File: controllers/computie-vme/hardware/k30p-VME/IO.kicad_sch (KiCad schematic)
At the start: 44 parts, among them J4 Serial1, J5 Serial2, P1 USB_C_Plug_USB2.0, P2 USB_C_Plug_USB2.0, SW3 E-Switch TL2243, U10 FT231XS, U3 74HC05, U8 MC68681, U9 FT231XS, Y2 Crystal

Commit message: Updating with more work in progress
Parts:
- removed JP2: IRQ, Connector_PinHeader_2.54mm:PinHeader_1x02_P2.54mm_Vertical, symbol Jumper:Jumper_2_Open
- removed JP3: ~{IACK}, Connector_PinHeader_2.54mm:PinHeader_1x02_P2.54mm_Vertical, symbol Jumper:Jumper_2_Open
- removed U3: 74HC05, Package_SO:TSSOP-14_4.4x5mm_P0.65mm, symbol 74xx:74LS05
- L1: value 600Ω @ 100MHz (MI0805K601R-10) -> MI0805K601R-10
- renumbered D5 to D2, D6 to D3, D3 to D4, D4 to D5, D7 to D6, D8 to D7, R16 to R12, R17 to R13, R18 to R14, R19 to R15, R12 to R16, R13 to R17, R14 to R18, R15 to R19, SW3 to SW2, P1 to USB1, P2 to USB2
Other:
- note added: "600Ω @ 100MHz"
- note added: "MC68681 DUAL SERIAL PORT CONTROLLER"
- note added: "SERIAL #1 FTDI SERIAL-TO-USB ADAPTER"
- note added: "SERIAL #2 FTDI SERIAL-TO-USB ADAPTER"
- note added: "TTL-LEVEL SERIAL DEBUG HEADERS"
- note removed: "TODO: remove these jumpers, rename the wires and use the priority encoder from the VME bus to generate the interrupts?"
- title: k30-VME32 -> k30p-VME
- moved on the sheet: C10, C11, C4, C5, C6, C7, C8, C9, D2, D3, D4, D5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

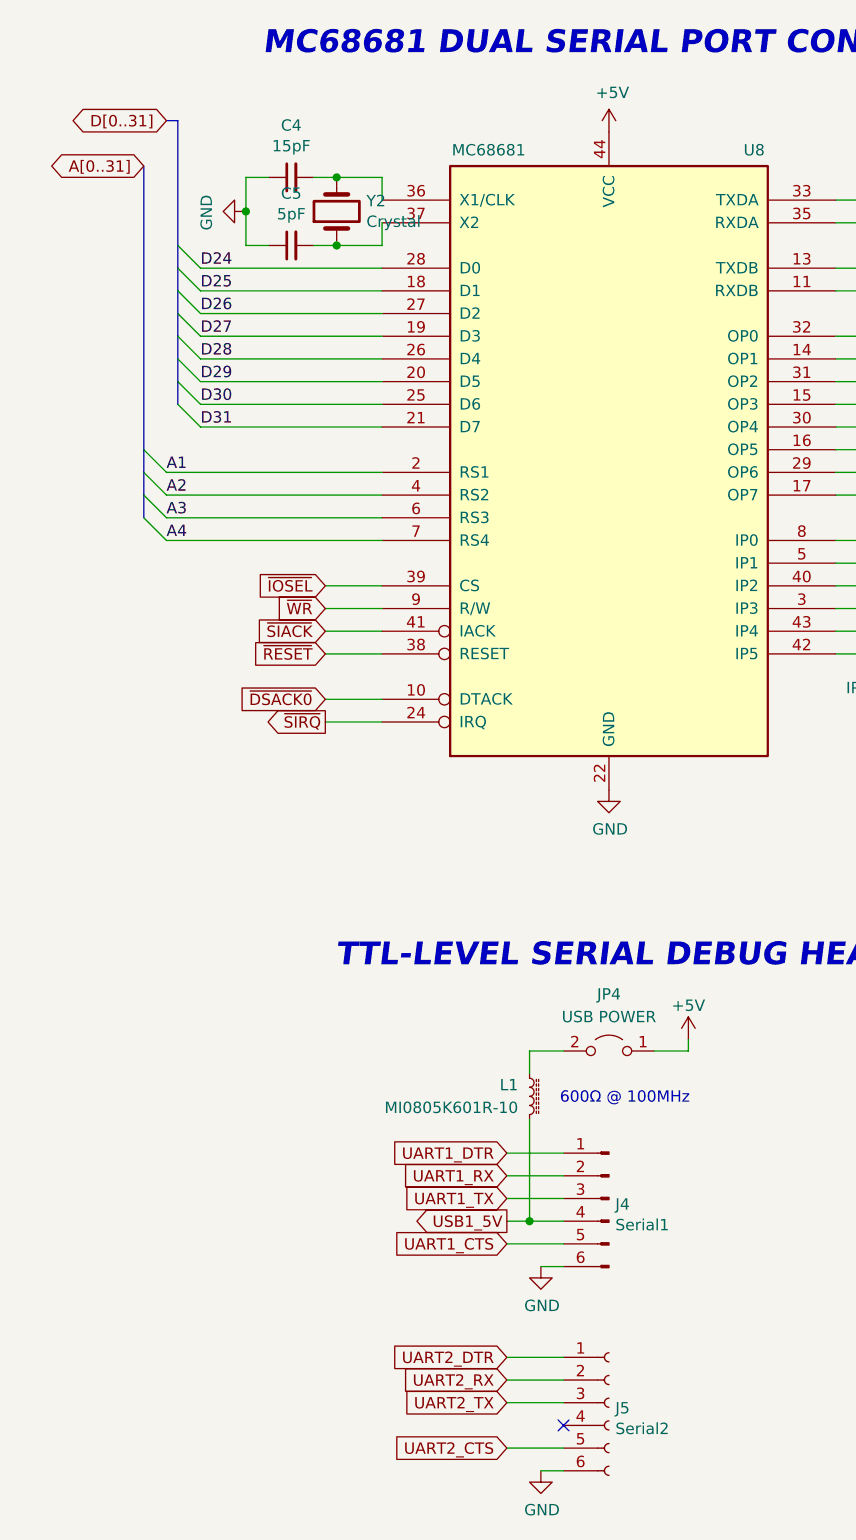
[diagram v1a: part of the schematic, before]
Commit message: Basic systemboard logic for bus arbitration is working and tested
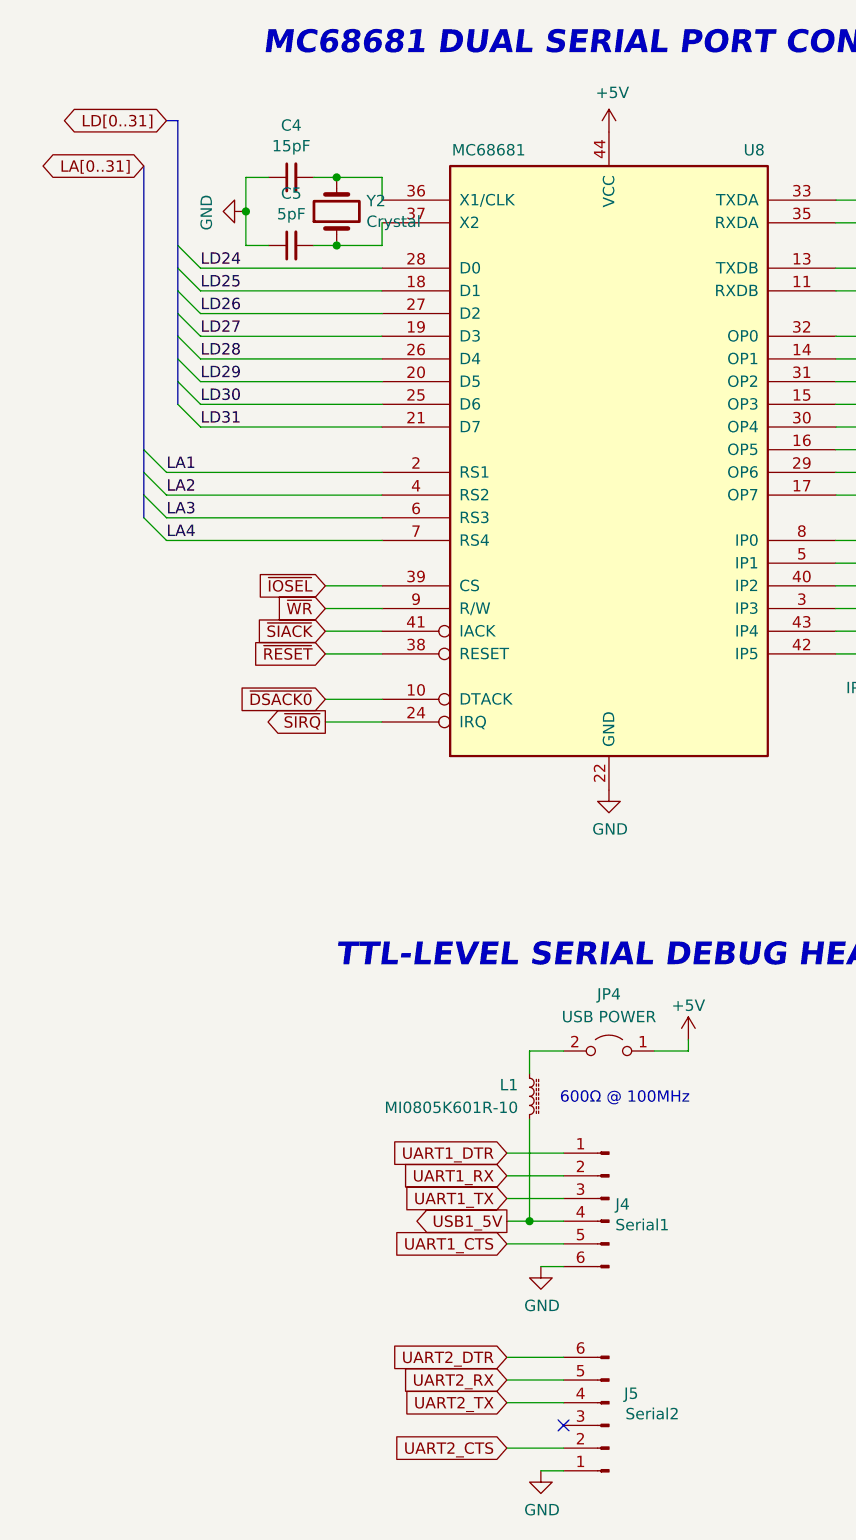
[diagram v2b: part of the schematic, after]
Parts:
- J4: symbol Connector:Conn_01x06_Male -> Connector:Conn_01x06_Pin
- J5: symbol Connector:Conn_01x06_Female -> Connector:Conn_01x06_Pin
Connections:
- net GND: now also J5.1 (Pin_1); no longer J5.6 (Pin_6)
- net UART2_CTS: now also J5.2 (Pin_2); no longer J5.5 (Pin_5)
- net UART2_DTR: now also J5.6 (Pin_6); no longer J5.1 (Pin_1)
- net UART2_RX: now also J5.5 (Pin_5); no longer J5.2 (Pin_2)
- net UART2_TX: now also J5.4 (Pin_4); no longer J5.3 (Pin_3)
- net A1 renamed LA1
- net A2 renamed LA2
- net A3 renamed LA3
- net A4 renamed LA4
- net D24 renamed LD24
- net D25 renamed LD25
- net D26 renamed LD26
- net D27 renamed LD27
- net D28 renamed LD28
- net D29 renamed LD29
- net D30 renamed LD30
- net D31 renamed LD31
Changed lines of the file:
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@@
 		)
 	)
-	(label "A1"
+	(label "LA1"
 		(at 29.21 68.58 0)
 		(fields_autoplaced yes)
@@
 		)
 	)
-	(label "A3"
+	(label "LA3"
 		(at 29.21 73.66 0)
 		(fields_autoplaced yes)
@@
 		)
 	)
-	(label "D31"
+	(label "LD31"
 		(at 33.02 63.5 0)
 		(fields_autoplaced yes)
@@
 		)
 	)
-	(label "A4"
+	(label "LA4"
 		(at 29.21 76.2 0)
 		(fields_autoplaced yes)
@@
 		)
 	)
-	(label "D26"
+	(label "LD26"
 		(at 33.02 50.8 0)
 		(fields_autoplaced yes)
@@
 		)
 	)
-	(label "D28"
+	(label "LD28"
 		(at 33.02 55.88 0)
 		(fields_autoplaced yes)
@@
 		)
 	)
-	(label "D29"
+	(label "LD29"
 		(at 33.02 58.42 0)
 		(fields_autoplaced yes)
@@
 		)
 	)
-	(label "D27"
+	(label "LD27"
 		(at 33.02 53.34 0)
 		(fields_autoplaced yes)
@@
 		)
 	)
-	(label "D30"
+	(label "LD30"
 		(at 33.02 60.96 0)
 		(fields_autoplaced yes)
@@
 		)
 	)
-	(label "A2"
+	(label "LA2"
 		(at 29.21 71.12 0)
 		(fields_autoplaced yes)
@@
 		)
 	)
-	(label "D25"
+	(label "LD25"
 		(at 33.02 48.26 0)
 		(fields_autoplaced yes)
@@
 		)
 	)
-	(label "D24"
+	(label "LD24"
 		(at 33.02 45.72 0)
 		(fields_autoplaced yes)
@@
 		)
 	)
-	(global_label "D[0..31]"
+	(global_label "LD[0..31]"
 		(shape tri_state)
 		(at 29.21 29.21 180)
@@
 		)
 		(property "Intersheetrefs" "${INTERSHEET_REFS}"
-			(at -41.91 6.35 0)
+			(at 16.2839 29.21 0)
 			(effects
 				(font
 					(size 1.27 1.27)
 				)
+				(justify right)
 				(hide yes)
 			)
@@
 		)
 	)
-	(global_label "A[0..31]"
+	(global_label "LA[0..31]"
 		(shape tri_state)
 		(at 26.67 34.29 180)
@@
 		)
 		(property "Intersheetrefs" "${INTERSHEET_REFS}"
-			(at -44.45 6.35 0)
+			(at 13.9253 34.29 0)
 			(effects
 				(font
 					(size 1.27 1.27)
 				)
+				(justify right)
 				(hide yes)
 			)
@@
 		)
 		(property "Netclass" "USB"
-			(at 253.3015 46.99 0)
+			(at 254.6985 46.99 0)
 			(effects
 				(font
@@
 					(italic yes)
 				)
-				(justify right)
+				(justify left)
 			)
 		)
@@
 			)
 		)
-		(property "Description" ""
+		(property "Description" "Power symbol creates a global label with name \"+5V\""
 			(at 78.74 30.48 0)
 			(effects
@@
 			)
 		)
-		(property "Description" ""
+		(property "Description" "Power symbol creates a global label with name \"GND\" , ground"
 			(at 78.74 104.14 0)
 			(effects
@@
 			)
 		)
-		(property "Description" ""
+		(property "Description" "Power symbol creates a global label with name \"GND\" , ground"
 			(at 38.1 39.37 0)
 			(effects
@@
 	)
 	(symbol
-		(lib_id "Connector:Conn_01x06_Male")
+		(lib_id "Connector:Conn_01x06_Pin")
 		(at 78.74 149.86 0)
 		(mirror y)
@@
 			)
 		)
-		(property "Description" ""
+		(property "Description" "Generic connector, single row, 01x06, script generated"
 			(at 78.74 149.86 0)
 			(effects
@@
 			)
 		)
-		(property "Description" ""
+		(property "Description" "Power symbol creates a global label with name \"GND\" , ground"
 			(at 71.12 180.34 0)
 			(effects
@@
 			)
 		)
-		(property "Description" ""
+		(property "Description" "Power symbol creates a global label with name \"GND\" , ground"
 			(at 71.12 157.48 0)
 			(effects
@@
 	)
 	(symbol
-		(lib_id "Connector:Conn_01x06_Female")
-		(at 78.74 172.72 0)
+		(lib_id "Connector:Conn_01x06_Pin")
+		(at 78.74 175.26 180)
 		(unit 1)
 		(exclude_from_sim no)
@@
 		(dnp no)
 		(property "Reference" "J5"
-			(at 79.4512 173.3296 0)
+			(at 82.042 171.704 0)
 			(effects
 				(font
@@
 		)
 		(property "Value" "Serial2"
-			(at 79.4512 175.641 0)
+			(at 86.614 173.99 0)
 			(effects
 				(font
@@
 		)
 		(property "Footprint" "Connector_PinHeader_2.54mm:PinHeader_1x06_P2.54mm_Vertical"
-			(at 78.74 172.72 0)
+			(at 78.74 175.26 0)
 			(effects
 				(font
@@
 		)
 		(property "Datasheet" "~"
-			(at 78.74 172.72 0)
+			(at 78.74 175.26 0)
 			(effects
 				(font
@@
 			)
 		)
-		(property "Description" ""
-			(at 78.74 172.72 0)
+		(property "Description" "Generic connector, single row, 01x06, script generated"
+			(at 78.74 175.26 0)
 			(effects
 				(font
@@
 			)
 		)
-		(property "Description" ""
+		(property "Description" "Power symbol creates a global label with name \"+5V\""
 			(at 163.83 54.61 0)
 			(effects
@@
 			)
 		)
-		(property "Description" ""
+		(property "Description" "Power symbol creates a global label with name \"+5V\""
 			(at 140.97 87.63 0)
 			(effects
@@
 			)
 		)
-		(property "Description" ""
+		(property "Description" "Power symbol creates a global label with name \"GND\" , ground"
 			(at 120.65 102.87 0)
 			(effects
@@
 			)
 		)
-		(property "Description" ""
+		(property "Description" "Power symbol creates a global label with name \"GND\" , ground"
 			(at 240.03 105.41 0)
 			(effects
@@
 			)
 		)
-		(property "Description" ""
+		(property "Description" "Power symbol creates a global label with name \"+5V\""
 			(at 213.36 102.87 0)
 			(effects
@@
 			)
 		)
-		(property "Description" ""
+		(property "Description" "Power symbol creates a global label with name \"GND\" , ground"
 			(at 210.82 83.82 0)
 			(effects
@@
 			)
 		)
-		(property "Description" ""
+		(property "Description" "Power symbol creates a global label with name \"GND\" , ground"
 			(at 243.84 63.5 0)
 			(effects
@@
 			)
 		)
-		(property "Description" ""
+		(property "Description" "Power symbol creates a global label with name \"GND\" , ground"
 			(at 240.03 35.56 0)
 			(effects
@@
 			)
 		)
-		(property "Description" ""
+		(property "Description" "Power symbol creates a global label with name \"GND\" , ground"
 			(at 274.32 76.2 0)
 			(effects
@@
 			)
 		)
-		(property "Description" ""
+		(property "Description" "Power symbol creates a global label with name \"GND\" , ground"
 			(at 248.92 63.5 0)
 			(effects
@@
 			)
 		)
-		(property "Description" ""
+		(property "Description" "Power symbol creates a global label with name \"GND\" , ground"
 			(at 210.82 153.67 0)
 			(effects
@@
 			)
 		)
-		(property "Description" ""
+		(property "Description" "Power symbol creates a global label with name \"GND\" , ground"
 			(at 243.84 133.35 0)
 			(effects
@@
 			)
 		)
-		(property "Description" ""
+		(property "Description" "Power symbol creates a global label with name \"+5V\""
 			(at 213.36 33.02 0)
 			(effects
@@
 			)
 		)
-		(property "Description" ""
+		(property "Description" "Power symbol creates a global label with name \"GND\" , ground"
 			(at 274.32 146.05 0)
 			(effects
@@
 			)
 		)
-		(property "Description" ""
+		(property "Description" "Power symbol creates a global label with name \"GND\" , ground"
 			(at 248.92 133.35 0)
 			(effects
@@
 			)
 		)
-		(property "Description" ""
+		(property "Description" "Power symbol creates a global label with name \"+5V\""
 			(at 87.63 132.08 0)
 			(effects

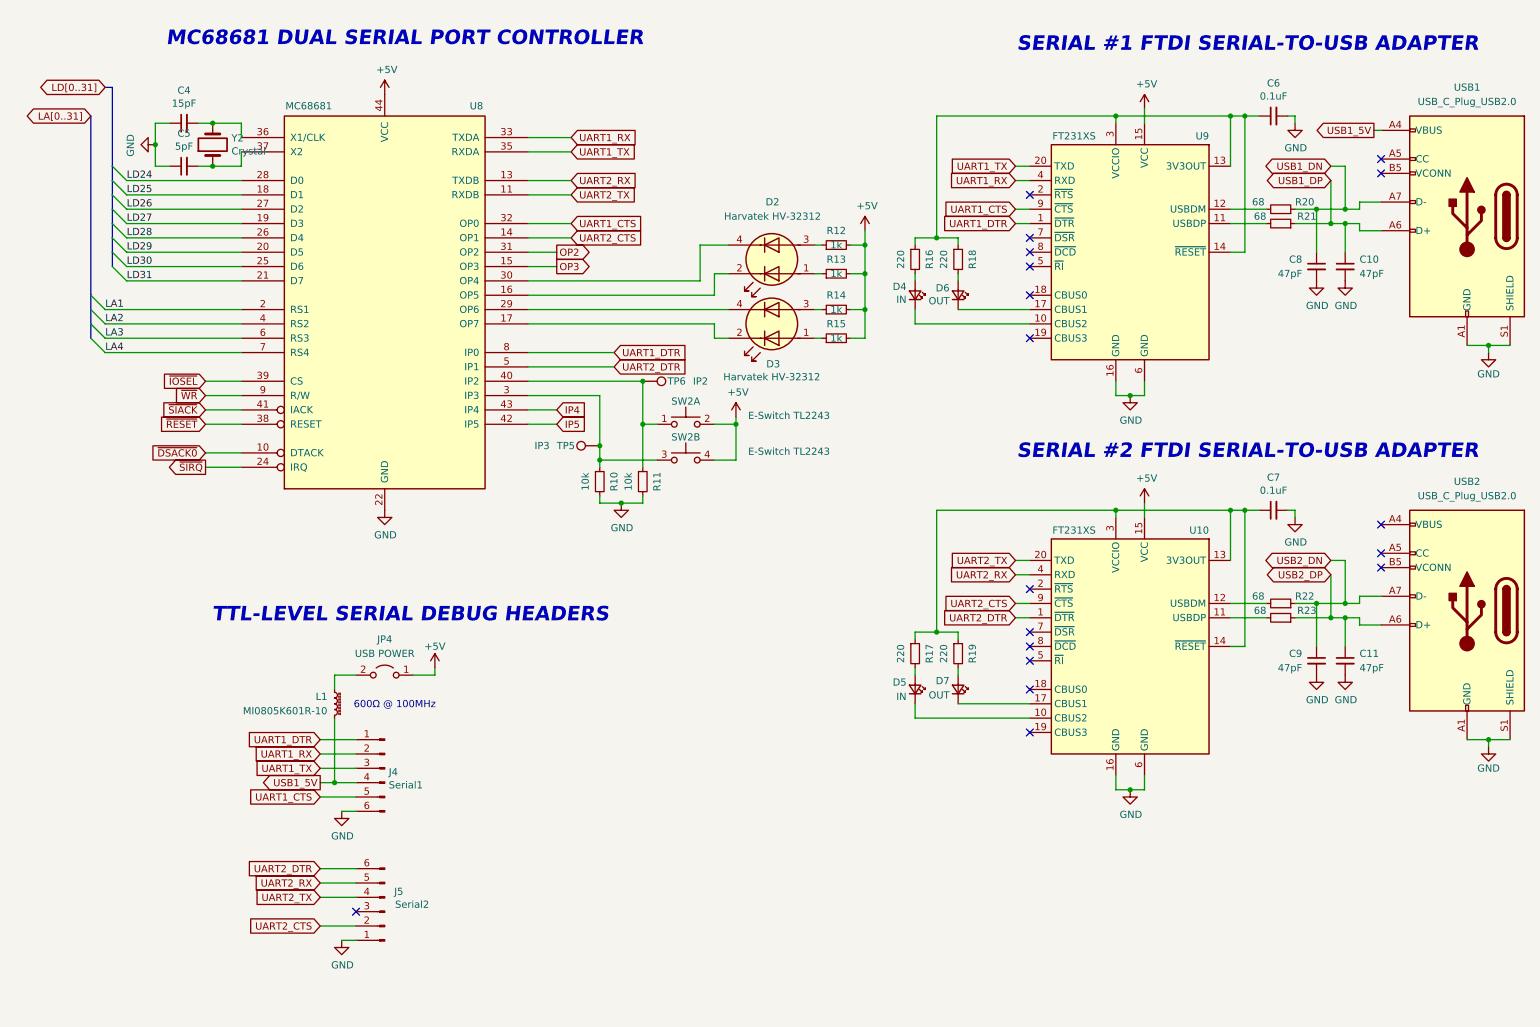
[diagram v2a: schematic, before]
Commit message: Mostly finished k30p-VME board and frontpanel
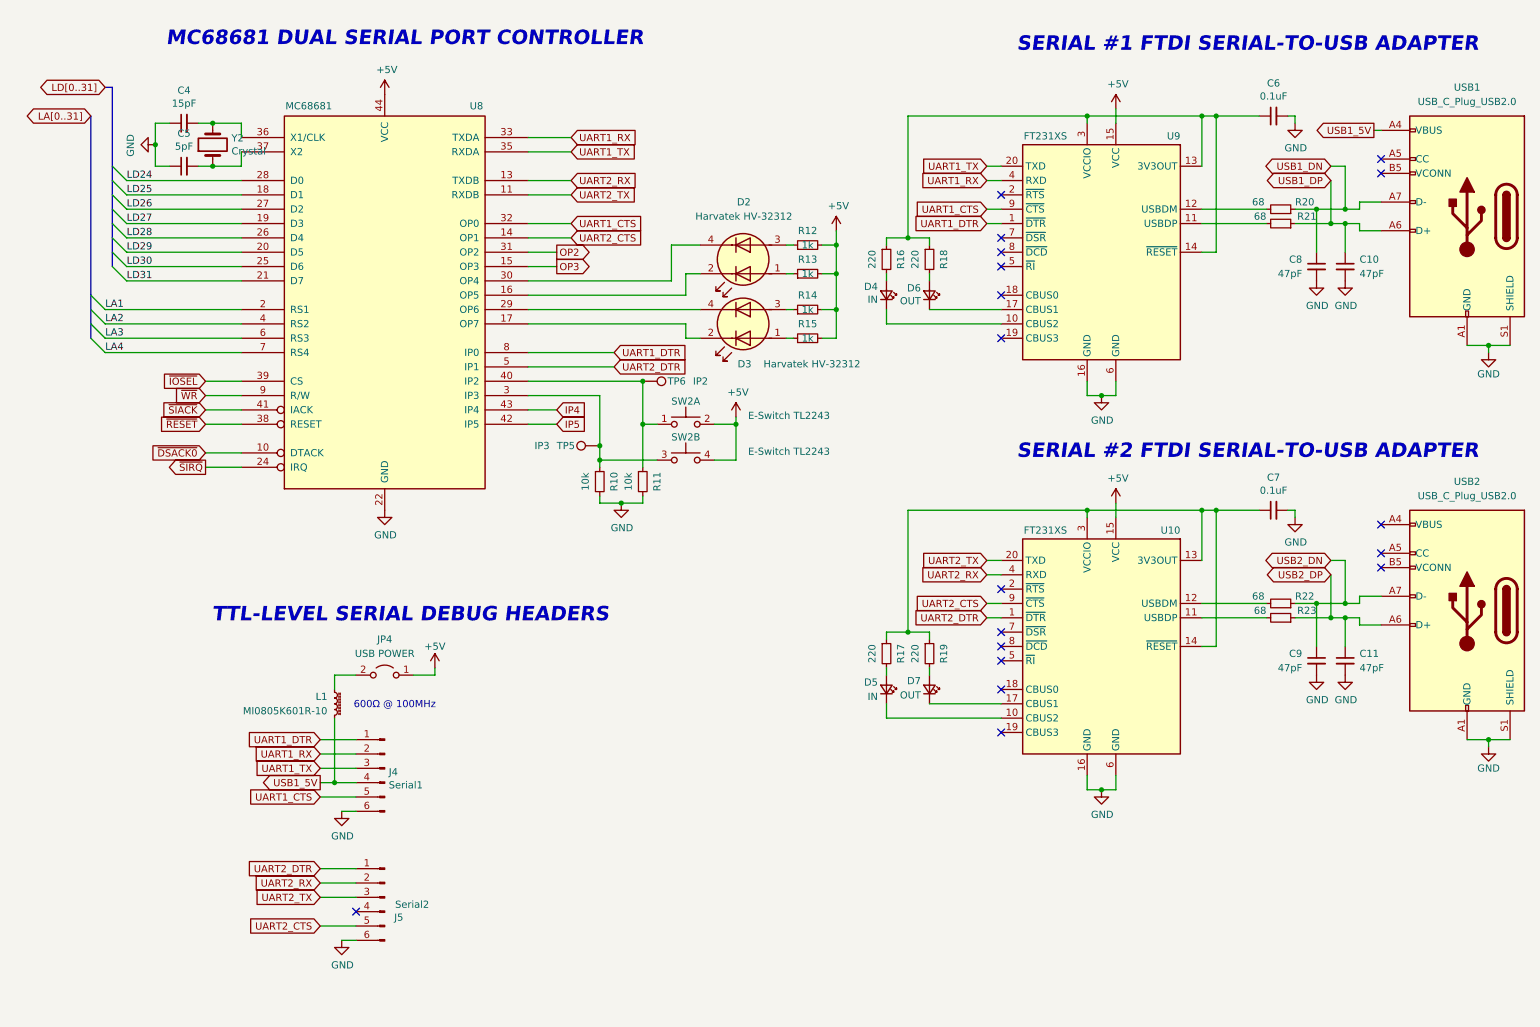
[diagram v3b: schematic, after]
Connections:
- net GND: now also J5.6 (Pin_6); no longer J5.1 (Pin_1)
- net UART2_CTS: now also J5.5 (Pin_5); no longer J5.2 (Pin_2)
- net UART2_DTR: now also J5.1 (Pin_1); no longer J5.6 (Pin_6)
- net UART2_RX: now also J5.2 (Pin_2); no longer J5.5 (Pin_5)
- net UART2_TX: now also J5.3 (Pin_3); no longer J5.4 (Pin_4)
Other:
- moved on the sheet: D2, D3, D4, D5, D6, D7, J5, R12, R13, R14, R15, R16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

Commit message: Added MemBird - Woodcock (16-bit VME memory card)
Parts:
- D4, D5, D6, D7: footprint LED_SMD:LED_1206_3216Metric_Pad1.42x1.75mm_HandSolder -> LED_SMD:LED_0805_2012Metric_Pad1.15x1.40mm_HandSolder
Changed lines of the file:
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@@
 			)
 		)
-		(property "Footprint" "LED_SMD:LED_1206_3216Metric_Pad1.42x1.75mm_HandSolder"
+		(property "Footprint" "LED_SMD:LED_0805_2012Metric_Pad1.15x1.40mm_HandSolder"
 			(at 175.26 135.89 90)
 			(effects
@@
 			)
 		)
-		(property "Footprint" "LED_SMD:LED_1206_3216Metric_Pad1.42x1.75mm_HandSolder"
+		(property "Footprint" "LED_SMD:LED_0805_2012Metric_Pad1.15x1.40mm_HandSolder"
 			(at 175.26 66.04 90)
 			(effects
@@
 			)
 		)
-		(property "Footprint" "LED_SMD:LED_1206_3216Metric_Pad1.42x1.75mm_HandSolder"
+		(property "Footprint" "LED_SMD:LED_0805_2012Metric_Pad1.15x1.40mm_HandSolder"
 			(at 167.64 66.04 90)
 			(effects
@@
 			)
 		)
-		(property "Footprint" "LED_SMD:LED_1206_3216Metric_Pad1.42x1.75mm_HandSolder"
+		(property "Footprint" "LED_SMD:LED_0805_2012Metric_Pad1.15x1.40mm_HandSolder"
 			(at 167.64 135.89 90)
 			(effects

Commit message: k30p-VME rev.1, MemBird Woodcock rev.1, and frontpanels
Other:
- moved on the sheet: C4, C5, R10, R11, SW2A, SW2B, TP5, TP6, U8, Y2
